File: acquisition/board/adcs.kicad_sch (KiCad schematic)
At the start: 107 parts, among them U1 AD9251, U2 XC7A50T-1FTG256C, U3 AD9251, U4 AD9251, U5 AD9251, U6 ICE40UP5K_QFN48

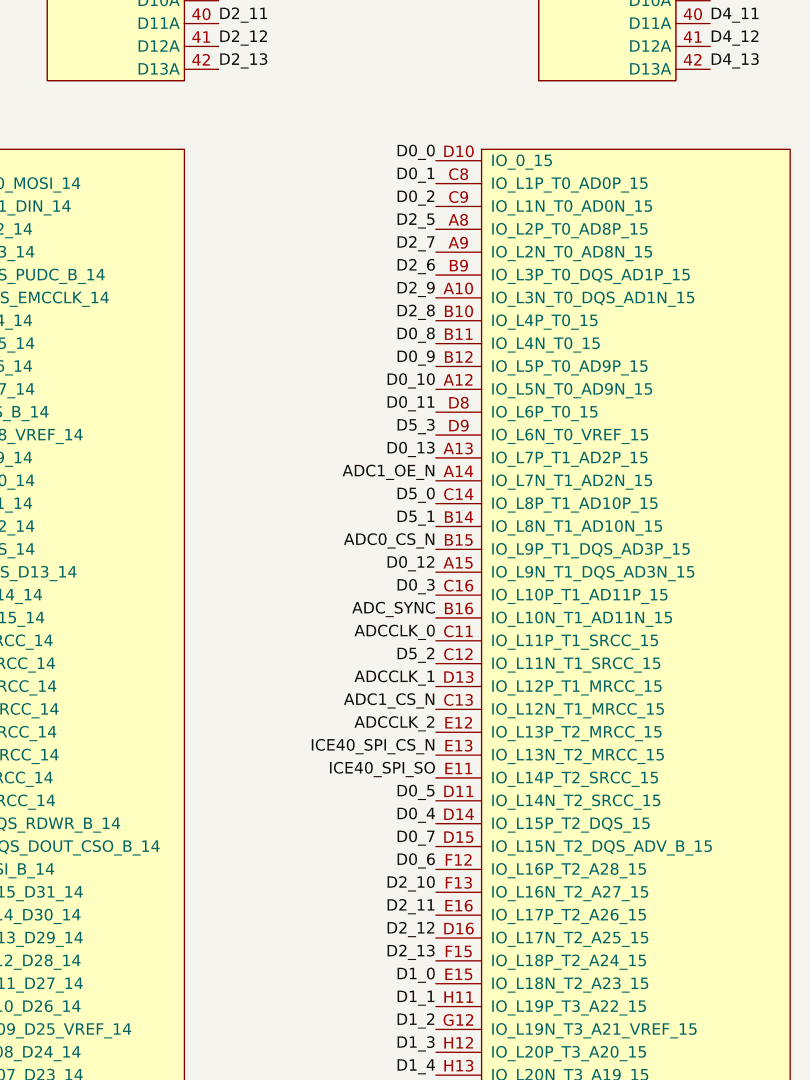
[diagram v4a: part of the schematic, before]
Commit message: Fully routed ADC #3
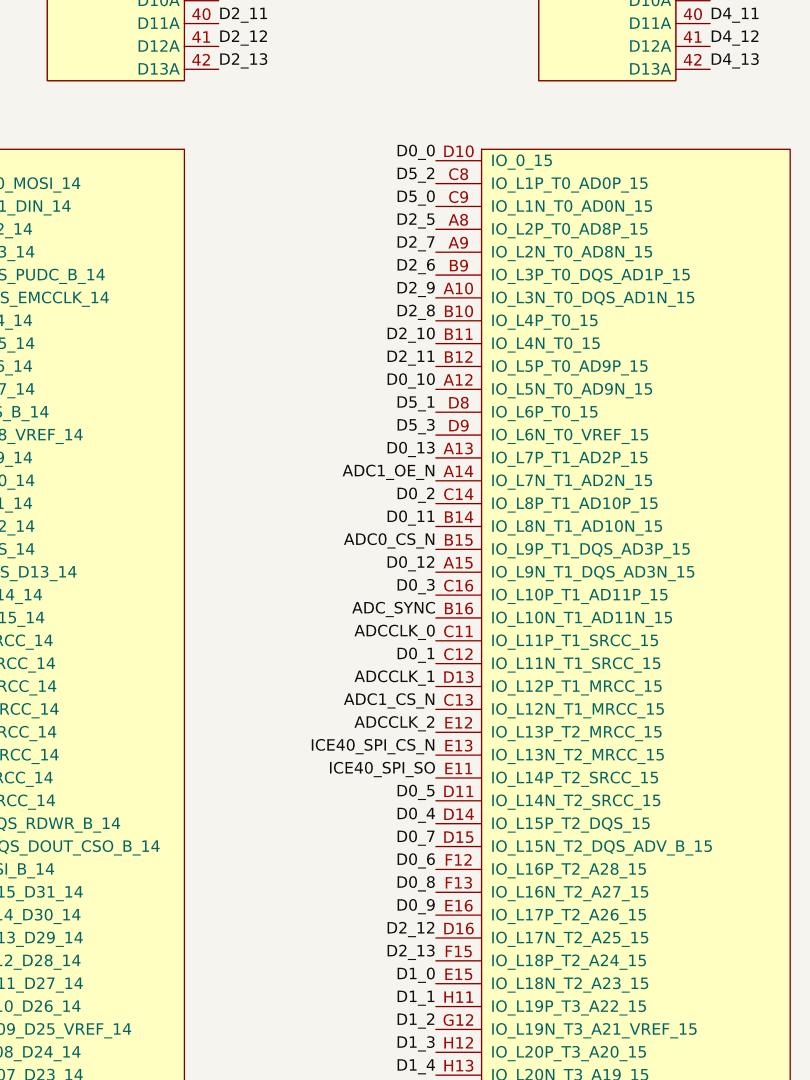
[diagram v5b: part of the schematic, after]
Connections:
- net D0_1: now also U2.C12 (IO_L11N_T1_SRCC_15); no longer U2.C8 (IO_L1P_T0_AD0P_15)
- net D0_11: now also U2.B14 (IO_L8N_T1_AD10N_15); no longer U2.D8 (IO_L6P_T0_15)
- net D0_2: now also U2.C14 (IO_L8P_T1_AD10P_15); no longer U2.C9 (IO_L1N_T0_AD0N_15)
- net D0_8: now also U2.F13 (IO_L16N_T2_A27_15); no longer U2.B11 (IO_L4N_T0_15)
- net D0_9: now also U2.E16 (IO_L17P_T2_A26_15); no longer U2.B12 (IO_L5P_T0_AD9P_15)
- net D2_10: now also U2.B11 (IO_L4N_T0_15); no longer U2.F13 (IO_L16N_T2_A27_15)
- net D2_11: now also U2.B12 (IO_L5P_T0_AD9P_15); no longer U2.E16 (IO_L17P_T2_A26_15)
- net D5_0: now also U2.C9 (IO_L1N_T0_AD0N_15); no longer U2.C14 (IO_L8P_T1_AD10P_15)
- net D5_1: now also U2.D8 (IO_L6P_T0_15); no longer U2.B14 (IO_L8N_T1_AD10N_15)
- net D5_2: now also U2.C8 (IO_L1P_T0_AD0P_15); no longer U2.C12 (IO_L11N_T1_SRCC_15)
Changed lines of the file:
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@@
     (effects (font (size 1.27 1.27)) (justify left bottom))
   )
-  (label "D0_2" (at 130.81 152.4 180)
+  (label "D0_2" (at 130.81 185.42 180)
     (effects (font (size 1.27 1.27)) (justify right bottom))
   )
@@
     (effects (font (size 1.27 1.27)) (justify right bottom))
   )
-  (label "D5_1" (at 130.81 187.96 180)
+  (label "D5_1" (at 130.81 175.26 180)
     (effects (font (size 1.27 1.27)) (justify right bottom))
   )
@@
     (effects (font (size 1.27 1.27)) (justify left bottom))
   )
-  (label "D0_8" (at 130.81 167.64 180)
+  (label "D0_8" (at 130.81 228.6 180)
     (effects (font (size 1.27 1.27)) (justify right bottom))
   )
@@
     (effects (font (size 1.27 1.27)) (justify left bottom))
   )
-  (label "D0_9" (at 130.81 170.18 180)
+  (label "D0_9" (at 130.81 231.14 180)
     (effects (font (size 1.27 1.27)) (justify right bottom))
   )
@@
     (effects (font (size 1.27 1.27)) (justify left bottom))
   )
-  (label "D0_11" (at 130.81 175.26 180)
+  (label "D0_11" (at 130.81 187.96 180)
     (effects (font (size 1.27 1.27)) (justify right bottom))
   )
@@
     (effects (font (size 1.27 1.27)) (justify right bottom))
   )
-  (label "D0_1" (at 130.81 149.86 180)
+  (label "D0_1" (at 130.81 203.2 180)
     (effects (font (size 1.27 1.27)) (justify right bottom))
   )
@@
     (effects (font (size 1.27 1.27)) (justify left bottom))
   )
-  (label "D2_10" (at 130.81 228.6 180)
+  (label "D2_10" (at 130.81 167.64 180)
     (effects (font (size 1.27 1.27)) (justify right bottom))
   )
@@
     (effects (font (size 1.27 1.27)) (justify left bottom))
   )
-  (label "D5_2" (at 130.81 203.2 180)
+  (label "D5_2" (at 130.81 149.86 180)
     (effects (font (size 1.27 1.27)) (justify right bottom))
   )
@@
     (effects (font (size 1.27 1.27)) (justify left bottom))
   )
-  (label "D2_11" (at 130.81 231.14 180)
+  (label "D2_11" (at 130.81 170.18 180)
     (effects (font (size 1.27 1.27)) (justify right bottom))
   )
@@
     (effects (font (size 1.27 1.27)) (justify right bottom))
   )
-  (label "D5_0" (at 130.81 185.42 180)
-    (effects (font (size 1.27 1.27)) (justify right bottom))
-  )
+  (label "D5_0" (at 130.81 152.4 180)
+    (effects (font (size 1.27 1.27)) (justify right bottom))
+  )
